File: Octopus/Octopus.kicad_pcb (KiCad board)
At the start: 2 copper layers, 205.8 x 111.7 mm, 88 parts, among them J1 MIDI IN (to panel DIN), J10 RN112BPC, J11 Button panel, J2 9-12VDC IN, J3 RN112BPC, J4 RN112BPC, J5 RN112BPC, J6 RN112BPC, J7 RN112BPC, J8 RN112BPC, J9 RN112BPC, K1 G5V-1, K10 G5V-1, K11 G5V-1, K12 G5V-1, K13 G5V-1, K14 G5V-1, K15 G5V-1, K16 G5V-1, K2 G5V-1, K3 G5V-1, K4 G5V-1, K5 G5V-1, K6 G5V-1, K7 G5V-1, K8 G5V-1, K9 G5V-1, U1 Teensy4.1, U2 6N138, U3 ULN2803A, U4 R-78E5.0-1.0, U5 ULN2803A

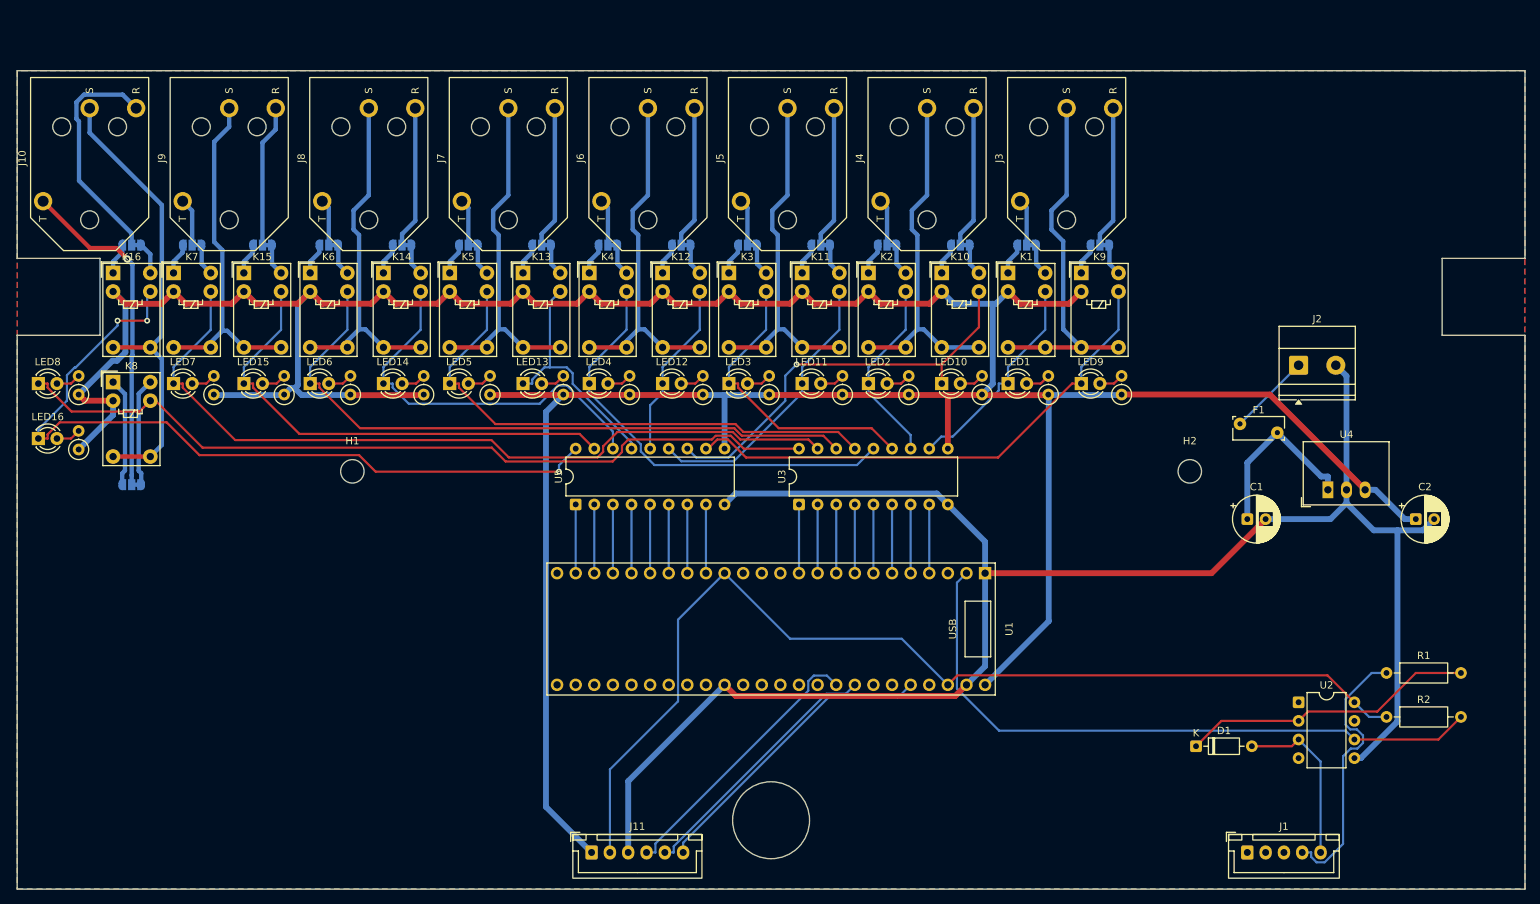
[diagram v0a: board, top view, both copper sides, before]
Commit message: Octopus: MIDI THRU, FM6725 DIN sockets, SnapMagic RN112BPC parts
- MIDI IN and a hardware MIDI THRU on two Cliff FM6725 right-angle DIN
  sockets through the back panel. THRU is buffered from the opto output
  by a 74HCT14 (two gates in series) into the standard 220R/220R 5 V
  source, independent of the firmware.
- Back panel re-planned around the sockets: jacks at 0.700" pitch, DIN
  holes beside jack 1, cord hole moved 3.67 mm; hole table in README.
- FM6725 footprint generated from the Cliff datasheet (tools/gen_din_fp.py)
  with the supplied 3D model.
- Jacks now use SnapMagic's RN112BPC symbol/footprint/3D model from
  case/RN112BPC via the project library tables (the vendor files are
  git-ignored: their licence doesn't allow redistribution).
- Mains PSU keep-free zone moved to the front right; jack 8's relays
  moved below the rear-post notch with a locked hand-routed tip run.
- ERC 0 errors; DRC 0 errors, 0 unconnected, 0 parity issues (16
  vendor silkscreen-at-edge warnings).

Co-Authored-By: Claude Opus 5.5 <noreply@anthropic.com>
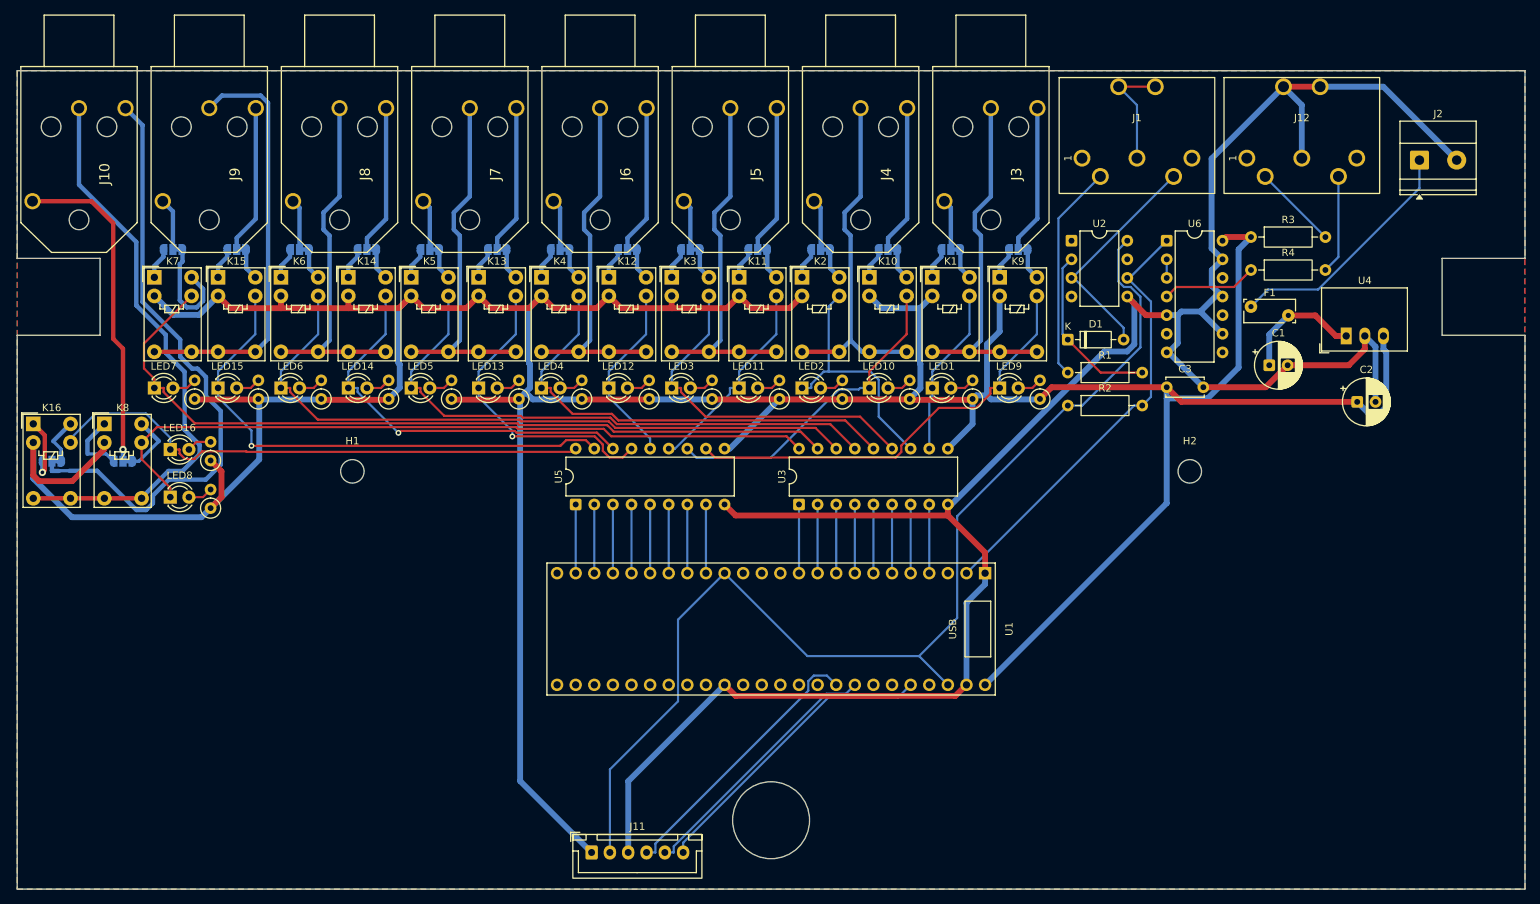
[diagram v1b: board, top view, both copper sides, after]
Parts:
- added C3: 100n, Capacitor_THT:C_Disc_D5.0mm_W2.5mm_P5.00mm, F.Cu at (204.0, 79.0)
- added J12: FM6725 MIDI THRU, Octopus:DIN-5_180deg_Cliff_FM6725_Horizontal, F.Cu at (222.4, 35.2)
- added R3: 220, Resistor_THT:R_Axial_DIN0207_L6.3mm_D2.5mm_P10.16mm_Horizontal, F.Cu at (215.5, 58.5)
- added R4: 220, Resistor_THT:R_Axial_DIN0207_L6.3mm_D2.5mm_P10.16mm_Horizontal, F.Cu at (215.5, 63.0)
- added U6: 74HCT14, Package_DIP:DIP-14_W7.62mm, F.Cu at (204.0, 59.0)
- J1: value MIDI IN (to panel DIN) -> FM6725 MIDI IN; footprint Connector_JST:JST_XH_B5B-XH-A_1x05_P2.50mm_Vertical -> Octopus:DIN-5_180deg_Cliff_FM6725_Horizontal
- J10, J3, J4, J5, J6, J7, J8, J9: footprint Octopus:Jack_6.35mm_Switchcraft_RN112BPC_Horizontal -> RN112BPC:SWITCHCRAFT_RN112BPC
- moved J1 108.3 mm to (199.9, 35.2), turned to 90 degrees
- moved U2 70.2 mm to (191.0, 59.0)
- moved R2 60.8 mm to (190.5, 81.5)
- moved R1 59.8 mm to (190.5, 77.0)
- moved D1 58.2 mm to (190.5, 72.5)
- moved J2 32.5 mm to (238.5, 48.0)
- moved JP16 31.4 mm to (51.8, 89.1)
- moved LED8 23.8 mm to (68.0, 94.0)
- moved R108 23.8 mm to (73.5, 95.5)
- moved K16 23.3 mm to (49.3, 84.0)
- moved C1 21.2 mm to (218.0, 76.0)
- moved U4 21.1 mm to (228.5, 72.0)
- moved LED16 18.1 mm to (68.0, 87.5)
- moved R116 18.1 mm to (73.5, 89.0)
- moved C2 17.9 mm to (230.0, 81.0)
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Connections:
- net Net-(D1-A) renamed /OPTO_K
- net Net-(D1-K) renamed /OPTO_A
- net Net-(J1-Pad4) renamed /MIDI_IN_4
- net Net-(U1-RX1) renamed /MIDI_RX
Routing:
- net +5V: track 497.2 -> 583.0 mm
- net GND: track 243.0 -> 303.3 mm
- net /CH16_OUT: track 32.0 -> 84.2 mm
- net /DRV16: track 108.0 -> 75.4 mm, vias 3 -> 0
- net /MIDI_RX: track 89.2 -> 60.1 mm
- net Net-(J2-Pin_1): track 11.3 -> 33.5 mm
- net /OPTO_A: track 40.3 -> 23.8 mm
- net unconnected-(J1-Pad2): track 0.00 -> 15.8 mm
- net /JACK8_SLV: track 63.8 -> 79.3 mm
- net /THRU_SINK: track 0.00 -> 13.5 mm
- net /DRV10: track 57.2 -> 44.0 mm, vias 1 -> 0
- net /THRU_TX: track 0.00 -> 13.0 mm
- net /THRU_SRC: track 0.00 -> 11.7 mm
- net /DRV8: track 112.5 -> 100.9 mm
- net /DRV9: track 71.6 -> 60.2 mm
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
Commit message: Octopus: front-panel display + encoder, Omron B3W-9 buttons, DigiKey BOM
- Button board: 0.96" SSD1306 OLED (Winstar WEA012864D-03 on 5 mm
  spacers) and an Alps EC11E15204A3 encoder with push switch, left of
  the buttons. MCP23008 -> MCP23017 for the extra inputs (GPA7/GPB7
  unused: output-only on current silicon).
- Buttons: the discontinued CTS 228C RGB switches are replaced by Omron
  B3W-9000-RG2N (red + green LEDs): red = tip, green = ring, amber =
  both. One PCA9685 instead of two; LED resistors are four Bourns CAT16
  4-resistor arrays. Square 10.6 mm panel cut-outs.
- Firmware: Display (U8g2/U8x8, redraws only what changed), encoder
  decoding from the MCP23017 interrupt (half-cycle detents), SELECT? /
  push-to-load / 5 s timeout, presets shown and entered as 1-128,
  MidiHandler::recall(), bigger Serial1 RX buffer.
- Main board: status LEDs and their resistors removed (the buttons show
  every line); C2 value corrected to 22 uF 16 V.
- BOM_DigiKey.csv: full parts list by manufacturer part number
  (force-added: the repo ignores *.csv).
- ERC 0 errors on both boards; DRC 0 errors, 0 unconnected, 0 parity
  (main board: 16 vendor-footprint silkscreen-at-edge warnings).

Co-Authored-By: Claude Opus 5.5 <noreply@anthropic.com>
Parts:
- removed LED1, LED10, LED11, LED12, LED13, LED14, LED15, LED16, LED2, LED3, LED4, LED5, LED6, LED7, LED8, LED9: LED, LED_THT:LED_D3.0mm
- removed R101, R102, R103, R104, R105, R106, R107, R108, R109, R110, R111, R112, R113, R114, R115, R116: 1k, Resistor_THT:R_Axial_DIN0207_L6.3mm_D2.5mm_P2.54mm_Vertical
- C2: value 22uF 10V -> 22uF 16V
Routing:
- net +5V: track 583.0 -> 461.4 mm
- net /CH16_OUT: track 84.2 -> 52.4 mm
- net /DRV15: track 72.0 -> 55.5 mm, vias 1 -> 0
- net /DRV14: track 54.7 -> 40.3 mm, vias 1 -> 0
- net /DRV13: track 41.7 -> 28.6 mm
- net /DRV4: track 63.7 -> 52.1 mm, vias 0 -> 1
- net +3V3: track 154.0 -> 165.3 mm
- net /CH15_NO: track 4.31 -> 14.9 mm
- net /DRV5: track 79.0 -> 69.5 mm
- net /DRV6: track 94.2 -> 85.4 mm
- net /DRV2: track 34.3 -> 26.0 mm
- net /DRV8: track 100.9 -> 93.3 mm
- net /DRV16: track 75.4 -> 70.2 mm
- net /DRV10: track 44.0 -> 39.3 mm, vias 0 -> 1
- net /JACK8_SLV: track 79.3 -> 83.1 mm, vias 0 -> 1
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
